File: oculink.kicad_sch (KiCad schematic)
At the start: 17 parts, among them J4 OCuLink_x4_Amphenol_G14A42121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, U10 ESD204DQAR, U11 ESD204DQAR, U8 ESD204DQAR, U9 ESD204DQAR

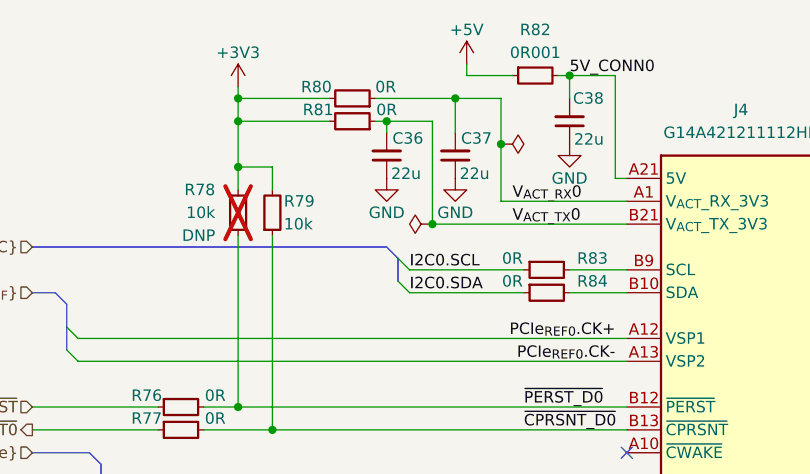
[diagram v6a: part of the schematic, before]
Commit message: Update components from the library
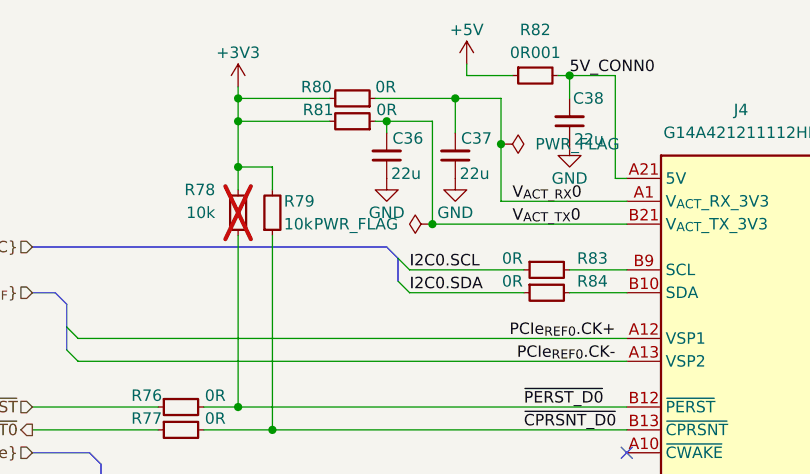
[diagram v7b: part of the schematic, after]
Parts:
- C36, C37, C38, R76, R77, R79, R80, R81, R82, R83, R84: Public (none) -> False
- R78: DNP DNP -> (none); Public (none) -> False
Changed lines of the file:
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@@
+      (effects (font (size 1.27 1.27)) (justify left bottom) hide)
+    )
+    (property "Public" "False" (at 264.16 74.93 0)
       (effects (font (size 1.27 1.27)) (justify left bottom) hide)
     )
@@
       (effects (font (size 1.27 1.27) (thickness 0.15)) (justify left bottom) hide)
     )
-    (property "Datasheet" "https://www.bourns.com/docs/product-datasheets/cr.pdf" (at 245.11 105.41 0)
+    (property "Datasheet" "https://www.eaton.com/content/dam/eaton/products/electronic-components/resources/data-sheet/eaton-msma-automotive-smd-current-sense-resistor-metal-strip-data-sheet-elx1179.pdf" (at 245.11 105.41 0)
       (effects (font (size 1.27 1.27) (thickness 0.15)) (justify left bottom) hide)
     )
@@
     )
     (property "Tolerance" "1%" (at 245.11 97.79 0)
+      (effects (font (size 1.27 1.27)) (justify left bottom) hide)
+    )
+    (property "Public" "False" (at 245.11 118.11 0)
       (effects (font (size 1.27 1.27)) (justify left bottom) hide)
     )
@@
       (effects (font (size 1.27 1.27) (thickness 0.15)) (justify left bottom) hide)
     )
+    (property "Public" "False" (at 189.23 62.23 0)
+      (effects (font (size 1.27 1.27)) (justify left bottom) hide)
+    )
     (pin "2")
     (pin "1")
@@
     (property "Current" "1A" (at 205.74 154.94 0)
       (effects (font (size 1.27 1.27) (thickness 0.15)) (justify left bottom) hide)
+    )
+    (property "Public" "False" (at 205.74 154.94 0)
+      (effects (font (size 1.27 1.27)) (justify left bottom) hide)
     )
     (pin "1")
@@
       (effects (font (size 1.27 1.27)) (justify left bottom) hide)
     )
+    (property "Public" "False" (at 243.84 78.74 0)
+      (effects (font (size 1.27 1.27)) (justify left bottom) hide)
+    )
     (pin "1")
     (pin "2")
@@
     (property "Current" "1A" (at 189.23 59.69 0)
       (effects (font (size 1.27 1.27) (thickness 0.15)) (justify left bottom) hide)
+    )
+    (property "Public" "False" (at 189.23 59.69 0)
+      (effects (font (size 1.27 1.27)) (justify left bottom) hide)
     )
     (pin "2")
@@
     )
     (property "Value" "PWR_FLAG" (at 227.33 95.2499 90)
-      (effects (font (size 1.27 1.27)) (justify left) hide)
+      (effects (font (size 1.27 1.27)) (justify left))
     )
     (property "Footprint" "" (at 223.52 95.25 0)
@@
       (effects (font (size 1.27 1.27)) (justify left bottom) hide)
     )
+    (property "Public" "False" (at 251.46 78.74 0)
+      (effects (font (size 1.27 1.27)) (justify left bottom) hide)
+    )
     (pin "1")
     (pin "2")
@@
     )
     (property "Value" "PWR_FLAG" (at 212.09 104.1399 90)
-      (effects (font (size 1.27 1.27)) (justify left) hide)
+      (effects (font (size 1.27 1.27)) (justify left))
     )
     (property "Footprint" "" (at 215.9 104.14 0)
@@
       (effects (font (size 1.27 1.27) (thickness 0.15)) (justify left bottom) hide)
     )
+    (property "Public" "False" (at 246.38 139.7 0)
+      (effects (font (size 1.27 1.27)) (justify left bottom) hide)
+    )
     (pin "2")
     (pin "1")
@@
       (effects (font (size 1.27 1.27)) (justify left bottom) hide)
     )
+    (property "Public" "False" (at 228.6 85.09 0)
+      (effects (font (size 1.27 1.27)) (justify left bottom) hide)
+    )
     (pin "2")
     (pin "1")
@@
     (property "Current" "1A" (at 205.74 157.48 0)
       (effects (font (size 1.27 1.27) (thickness 0.15)) (justify left bottom) hide)
+    )
+    (property "Public" "False" (at 205.74 157.48 0)
+      (effects (font (size 1.27 1.27)) (justify left bottom) hide)
     )
     (pin "1")
@@
       (effects (font (size 1.27 1.27)) (justify left bottom) hide)
     )
-    (property "DNP" "DNP" (at 191.77 105.41 90)
-      (effects (font (size 1.27 1.27)) (justify left))
+    (property "Public" "False" (at 224.79 85.09 0)
+      (effects (font (size 1.27 1.27)) (justify left bottom) hide)
     )
     (pin "2")
@@
       (effects (font (size 1.27 1.27) (thickness 0.15)) (justify left bottom) hide)
     )
-    (pin "2")
+    (property "Public" "False" (at 246.38 142.24 0)
+      (effects (font (size 1.27 1.27)) (justify left bottom) hide)
+    )
+    (pin "2")

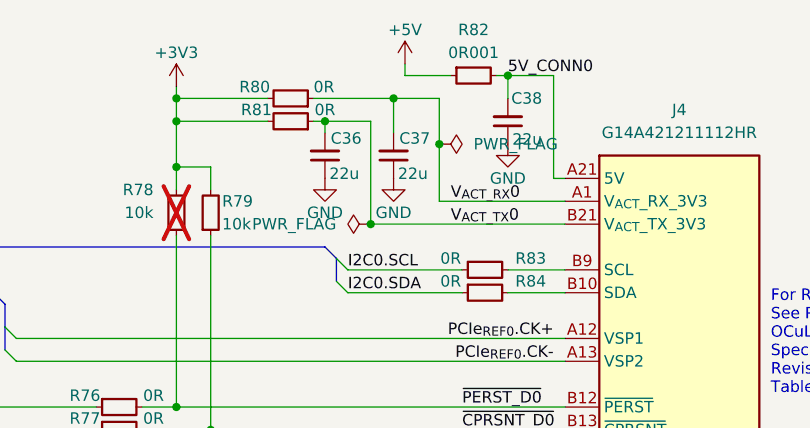
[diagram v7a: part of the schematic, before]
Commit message: [#65447] Fix rotated LEDs, overlapping text and symbols, add rules
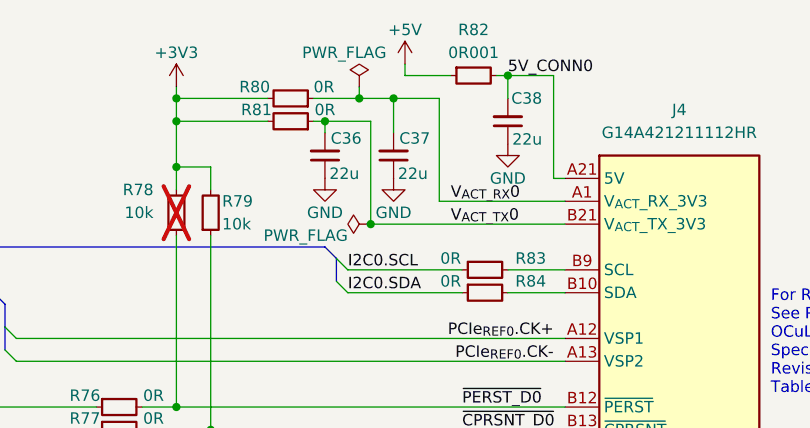
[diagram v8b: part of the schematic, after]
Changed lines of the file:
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@@
   (junction (at 210.82 92.71) (diameter 0) (color 0 0 0 0)
   )
+  (junction (at 214.63 90.17) (diameter 0) (color 0 0 0 0)
+  )
   (junction (at 194.31 92.71) (diameter 0) (color 0 0 0 0)
   )
   (junction (at 194.31 124.46) (diameter 0) (color 0 0 0 0)
-  )
-  (junction (at 223.52 95.25) (diameter 0) (color 0 0 0 0)
   )
   (junction (at 264.16 190.5) (diameter 0) (color 0 0 0 0)
@@
     (stroke (width 0) (type default))
   )
-  (wire (pts (xy 223.52 101.6) (xy 223.52 95.25))
+  (wire (pts (xy 223.52 90.17) (xy 223.52 101.6))
     (stroke (width 0) (type default))
   )
@@
     (stroke (width 0) (type default))
   )
-  (wire (pts (xy 223.52 95.25) (xy 223.52 90.17))
-    (stroke (width 0) (type default))
-  )
   (wire (pts (xy 180.34 175.26) (xy 237.49 175.26))
     (stroke (width 0) (type default))
@@
     (stroke (width 0) (type default))
   )
+  (wire (pts (xy 214.63 88.9) (xy 214.63 90.17))
+    (stroke (width 0) (type default))
+  )
   (wire (pts (xy 180.34 165.1) (xy 237.49 165.1))
     (stroke (width 0) (type default))
@@
     (stroke (width 0) (type default))
   )
-  (wire (pts (xy 209.55 90.17) (xy 218.44 90.17))
+  (wire (pts (xy 209.55 90.17) (xy 214.63 90.17))
     (stroke (width 0) (type default))
   )
@@
   )
   (wire (pts (xy 176.53 116.84) (xy 237.49 116.84))
+    (stroke (width 0) (type default))
+  )
+  (wire (pts (xy 214.63 90.17) (xy 218.44 90.17))
     (stroke (width 0) (type default))
   )
@@
     )
   )
-  (symbol (lib_id "antmicropower:PWR_FLAG") (at 223.52 95.25 270) (unit 1)
-    (in_bom yes) (on_board yes) (dnp no) (fields_autoplaced)
-    (property "Reference" "#FLG04" (at 225.425 95.25 0)
+  (symbol (lib_id "antmicropower:PWR_FLAG") (at 214.63 88.9 0) (unit 1)
+    (in_bom yes) (on_board yes) (dnp no)
+    (property "Reference" "#FLG04" (at 214.63 86.995 0)
       (effects (font (size 1.27 1.27)) hide)
     )
-    (property "Value" "PWR_FLAG" (at 227.33 95.2499 90)
+    (property "Value" "PWR_FLAG" (at 208.28 85.09 0)
       (effects (font (size 1.27 1.27)) (justify left))
     )
-    (property "Footprint" "" (at 223.52 95.25 0)
+    (property "Footprint" "" (at 214.63 88.9 0)
       (effects (font (size 1.27 1.27)) hide)
     )
-    (property "Datasheet" "" (at 223.52 95.25 0)
+    (property "Datasheet" "" (at 214.63 88.9 0)
       (effects (font (size 1.27 1.27)) hide)
     )
@@
   )
   (symbol (lib_id "antmicropower:PWR_FLAG") (at 215.9 104.14 90) (unit 1)
-    (in_bom yes) (on_board yes) (dnp no) (fields_autoplaced)
+    (in_bom yes) (on_board yes) (dnp no)
     (property "Reference" "#FLG03" (at 213.995 104.14 0)
       (effects (font (size 1.27 1.27)) hide)
     )
-    (property "Value" "PWR_FLAG" (at 212.09 104.1399 90)
+    (property "Value" "PWR_FLAG" (at 213.36 105.41 90)
       (effects (font (size 1.27 1.27)) (justify left))
     )
